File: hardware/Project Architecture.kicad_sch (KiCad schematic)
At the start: 0 parts

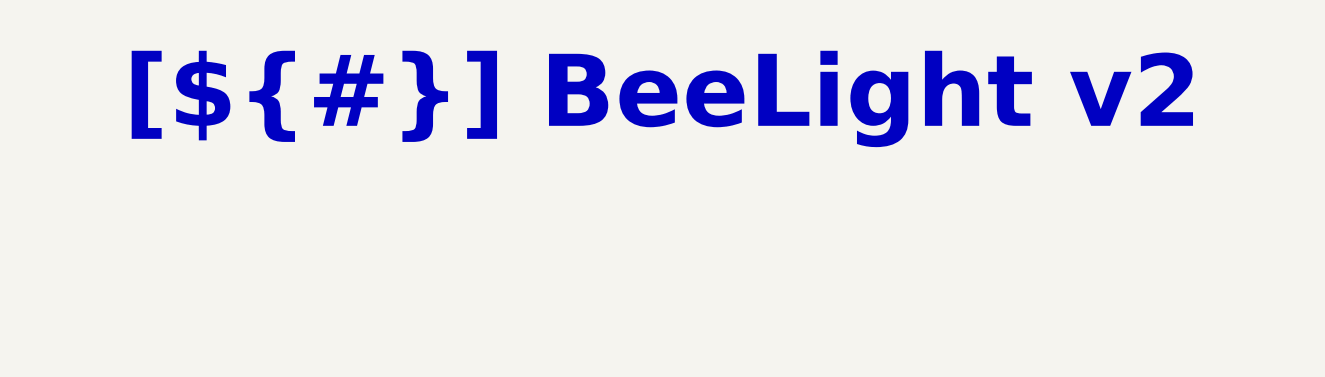
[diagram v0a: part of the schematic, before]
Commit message: Implement new CI/CD workflow
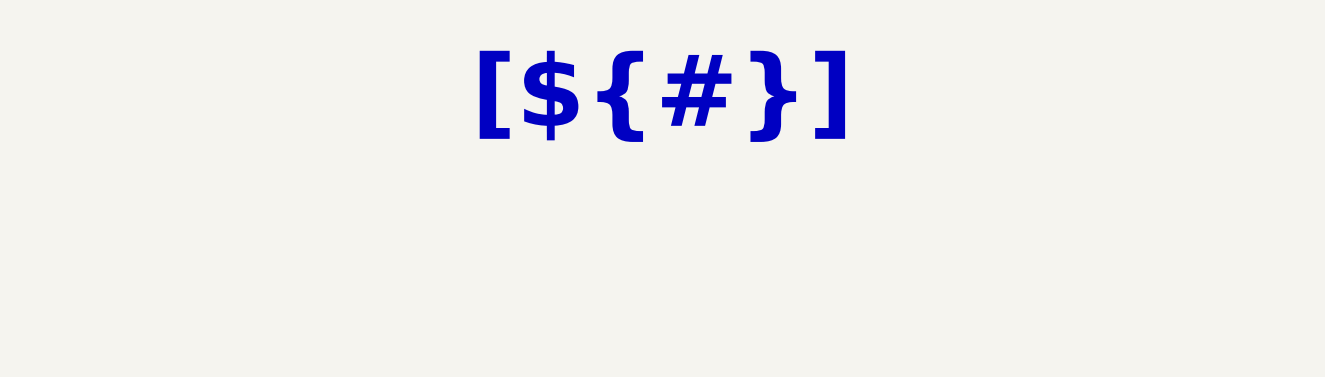
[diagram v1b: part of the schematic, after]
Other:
- title: BeeLight v2 -> (none)
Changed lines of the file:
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@@
 	(paper "A3")
 	(title_block
-		(title "BeeLight v2")
 		(date "2025-06-05")
 		(rev "${REVISION}")

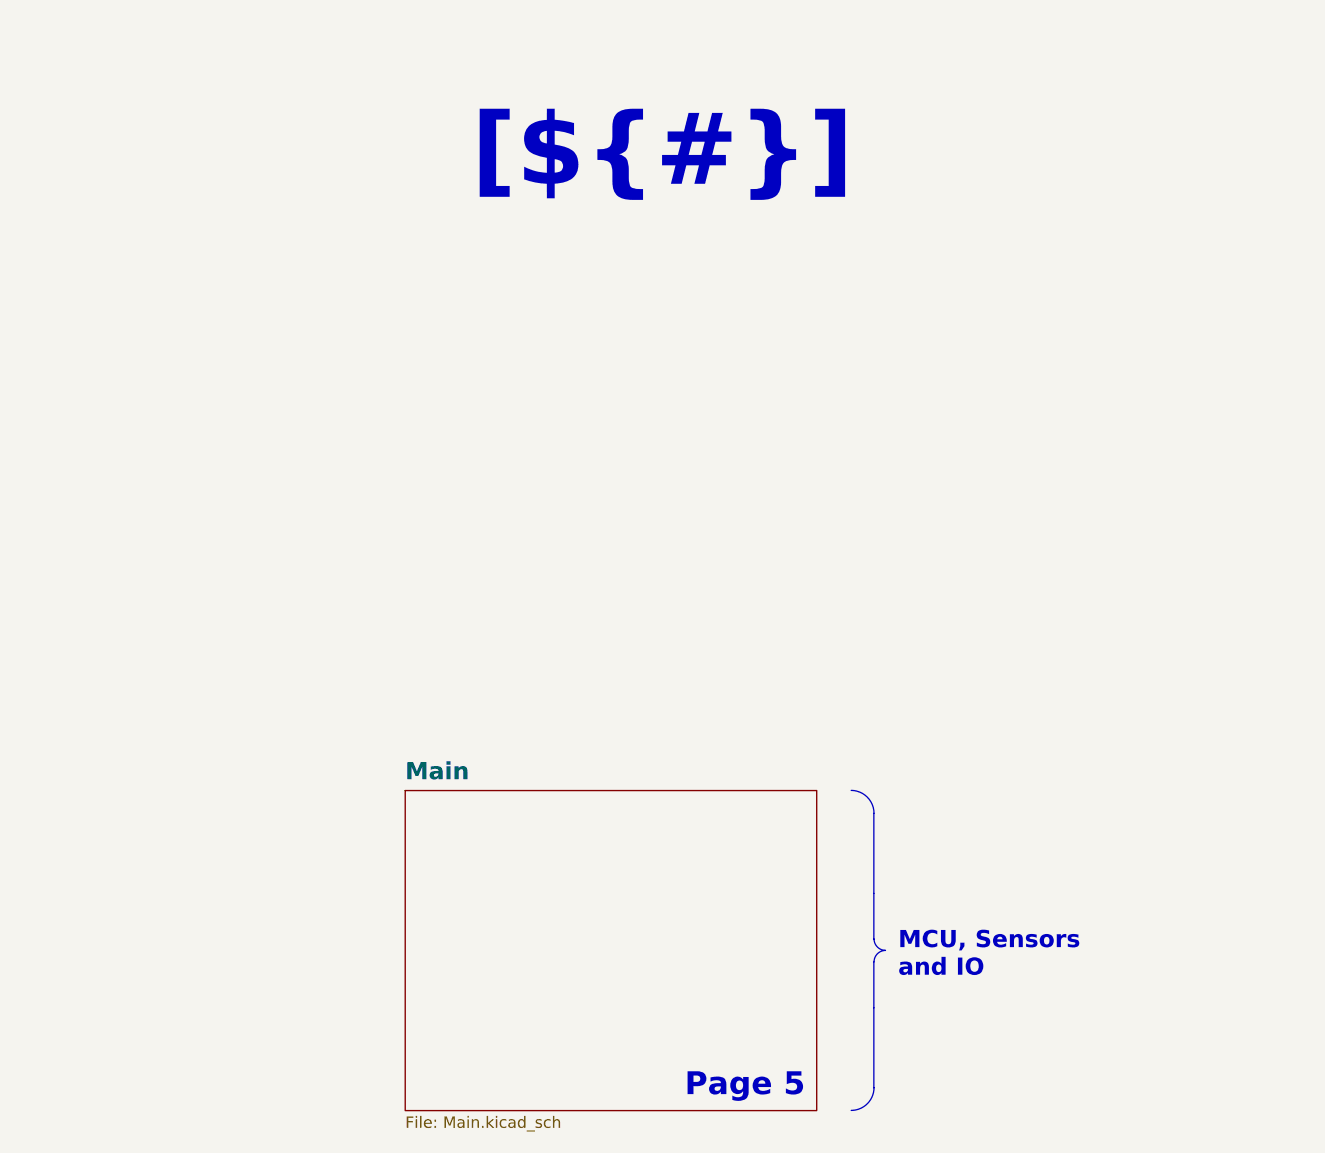
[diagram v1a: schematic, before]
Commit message: - Change ADC filter capacitor to 1 nF - Update documentation with current consumption - Update CI/CD pipeline
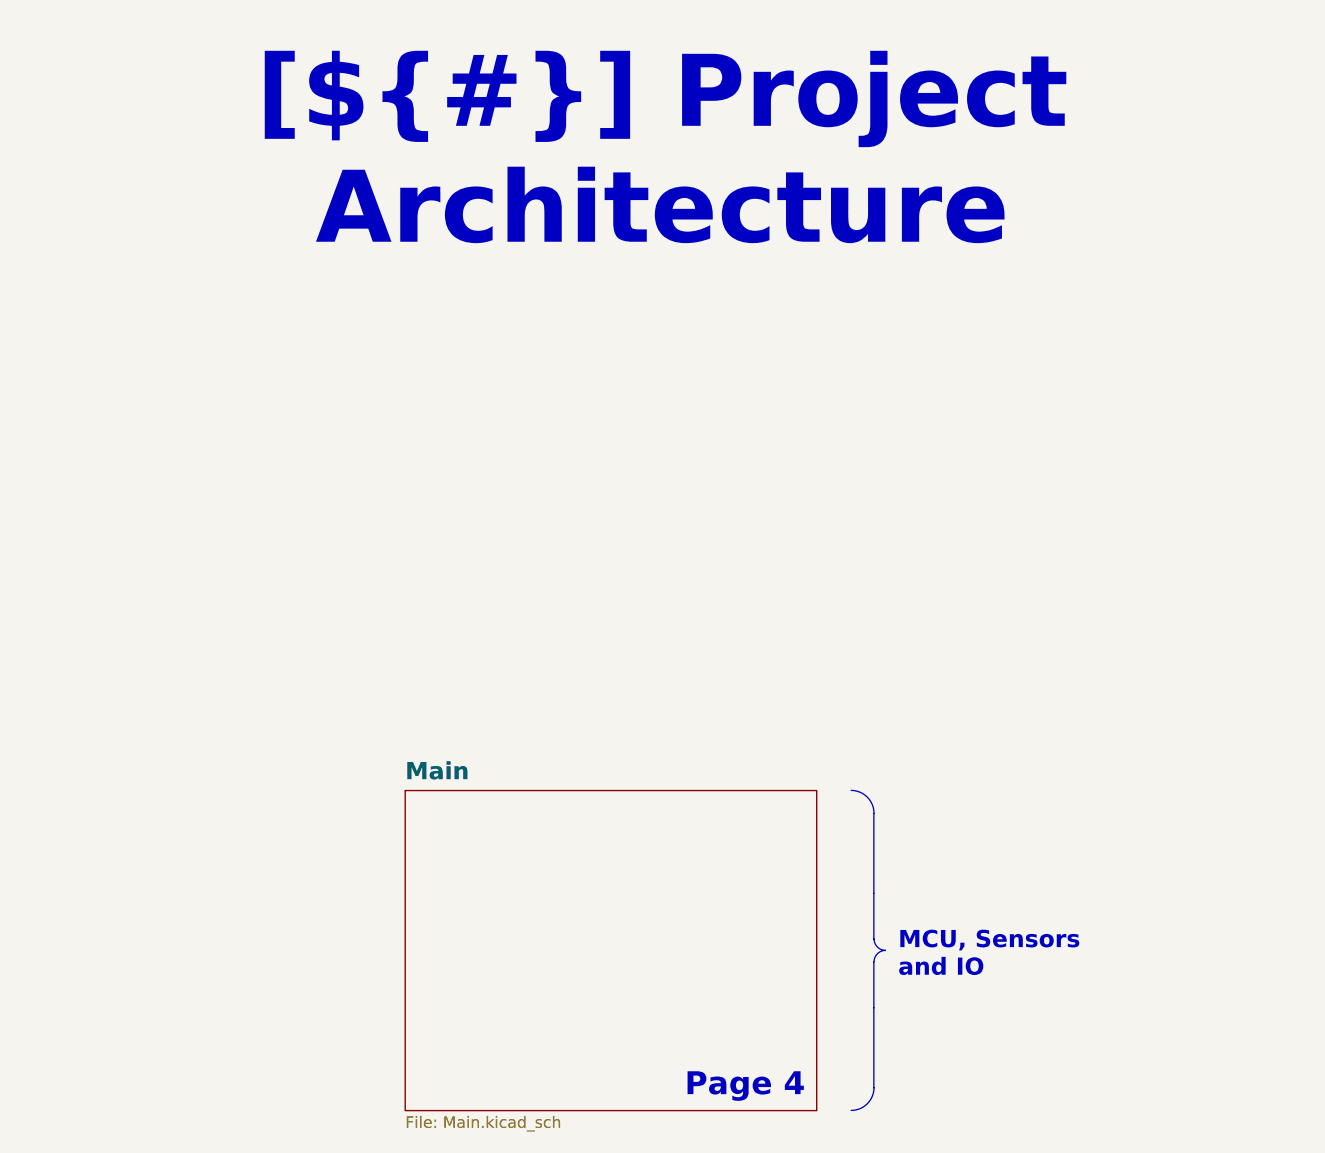
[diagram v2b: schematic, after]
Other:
- note added: "Page 4"
- note removed: "Page 5"
- title: (none) -> Project Architecture
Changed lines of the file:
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@@
 	(paper "A3")
 	(title_block
+		(title "Project Architecture")
 		(date "2025-06-05")
 		(rev "${REVISION}")
@@
 		)
 	)
-	(text "Page 5"
+	(text "Page 4"
 		(exclude_from_sim no)
 		(at 226.06 133.35 0)
@@
 		)
 		(instances
-			(project "KDT_Hierarchical_KiBot"
-				(path "/f9e05184-c88b-4a88-ae9c-ab2bdb32be7c/c5103ceb-5325-4a84-a025-9638a412984e"
-					(page "5")
-				)
-			)
 			(project "BeeLight"
 				(path "/d5742f03-3b1a-42e5-a384-018bd4b919aa/c5103ceb-5325-4a84-a025-9638a412984e"
